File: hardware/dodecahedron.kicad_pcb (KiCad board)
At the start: 2 copper layers, 100 x 86.6 mm, 49 parts, among them J1 Conn_01x04, J2 Conn_01x04, J3 Conn_01x04, J4 Conn_01x04, J5 Conn_01x04, J6 Conn_01x04

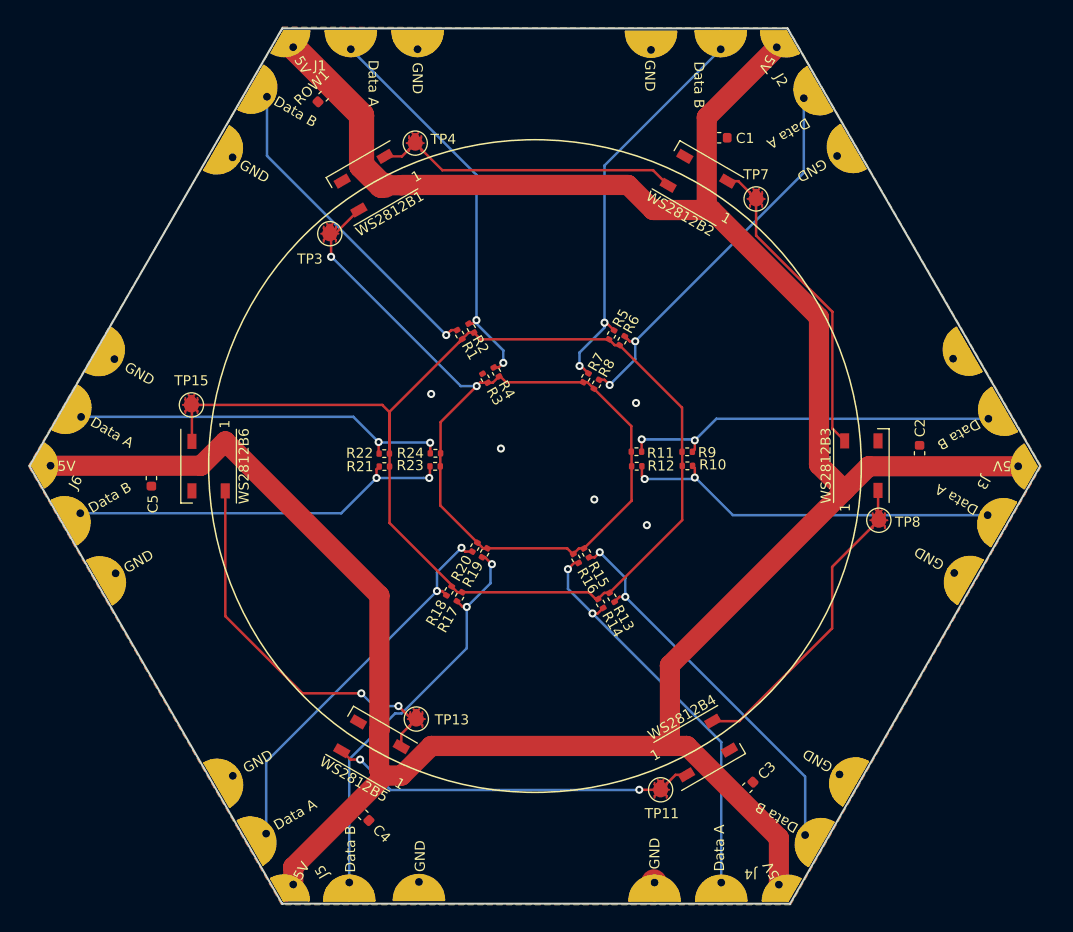
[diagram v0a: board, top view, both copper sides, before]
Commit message: Fixed up a rotated LED
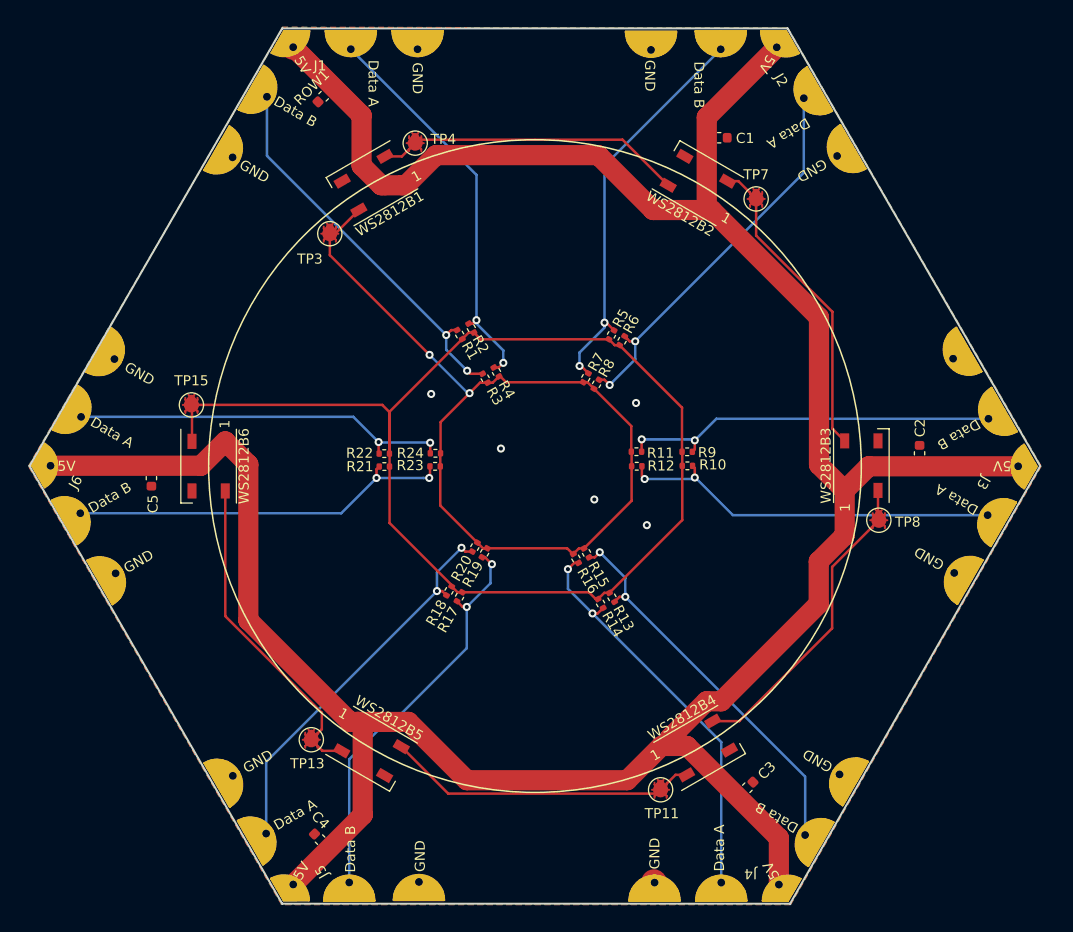
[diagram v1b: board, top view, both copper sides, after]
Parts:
- moved TP13 10.6 mm to (114.1, 162.4)
- moved C4 4.92 mm to (115.0, 172.3), turned to 135 degrees
- turned WS2812B5 to -30 degrees
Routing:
- net +5V: track 275.0 -> 282.1 mm
- net Net-(WS2812B5-DOU): track 38.9 -> 32.5 mm, vias 2 -> 0
- net Net-(J1-Pin_3): track 32.2 -> 38.2 mm, vias 1 -> 2
- net Net-(WS2812B4-DOU): track 36.3 -> 30.9 mm, vias 2 -> 0

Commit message: Added circles to the silk screen
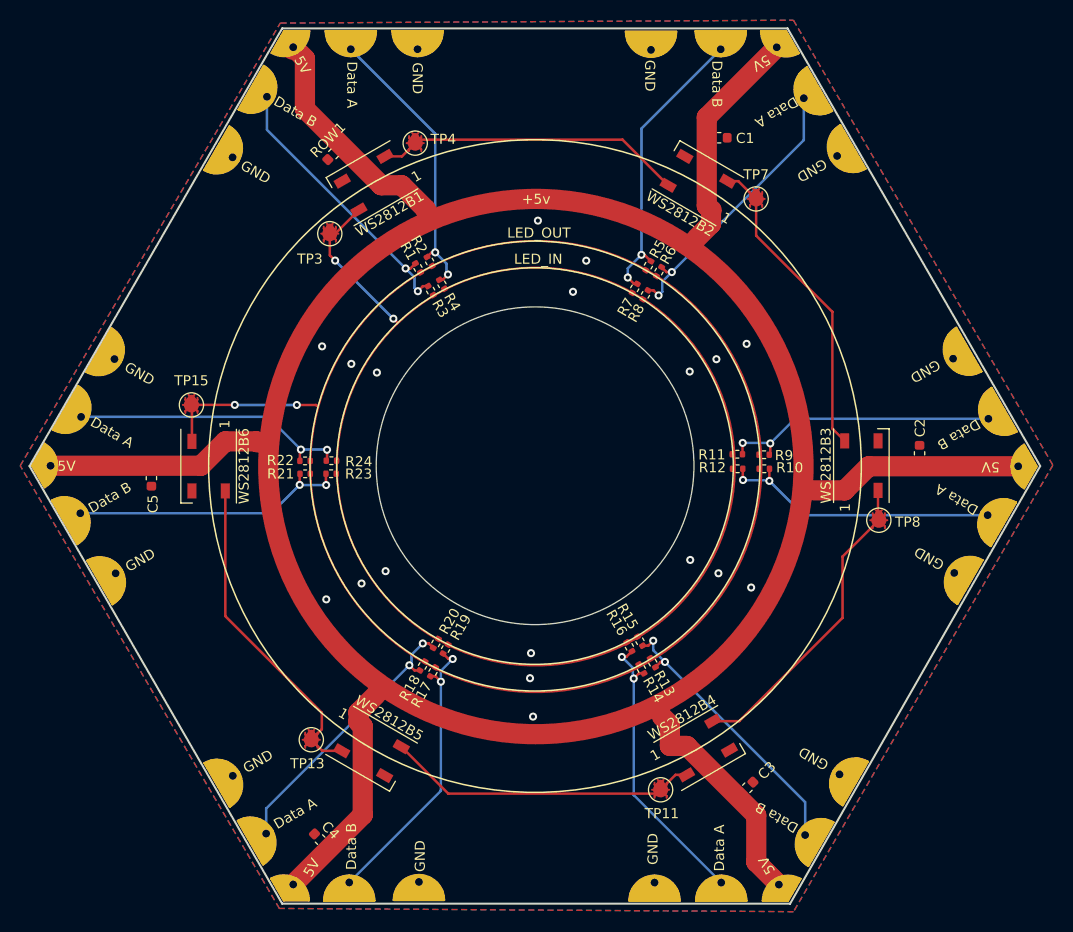
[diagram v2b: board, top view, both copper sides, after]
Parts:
- moved R23 10.3 mm to (116.1, 136.1)
- moved R24 10.3 mm to (116.1, 134.8)
- moved R19 10.3 mm to (127.4, 153.5)
- moved R20 10.3 mm to (126.5, 152.9)
- moved R15 10.2 mm to (146.7, 152.7)
- moved R16 10.2 mm to (145.6, 153.2)
- moved R3 10.2 mm to (125.9, 118.0)
- moved R4 10.2 mm to (127.1, 117.4)
- moved R7 10.1 mm to (146.1, 117.8)
- moved R8 10.1 mm to (147.2, 118.4)
- moved R11 9.98 mm to (156.3, 134.2)
- moved R12 9.98 mm to (156.3, 135.6)
- moved R17 7.88 mm to (126.2, 155.7)
- moved R18 7.88 mm to (125.1, 155.1)
- moved R21 7.87 mm to (113.5, 136.1)
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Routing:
- net +5V: track 282.1 -> 133.1 mm
- net LED_OUT: track 120.3 -> 16.0 mm, vias 0 -> 2
- net LED_IN: track 87.0 -> 15.3 mm
- net Net-(J5-Pin_3): track 40.2 -> 28.8 mm
- net Net-(J2-Pin_2): track 39.2 -> 27.9 mm
- net Net-(J4-Pin_3): track 38.9 -> 27.9 mm
- net Net-(J4-Pin_2): track 39.9 -> 28.8 mm
- net Net-(J1-Pin_2): track 39.3 -> 28.3 mm
- net Net-(J5-Pin_2): track 38.6 -> 27.7 mm
- net Net-(J2-Pin_3): track 39.6 -> 28.8 mm
- net Net-(J6-Pin_3): track 38.4 -> 27.7 mm
- net Net-(J1-Pin_3): track 38.2 -> 27.8 mm
- net Net-(J3-Pin_2): track 38.2 -> 28.0 mm
- net Net-(J3-Pin_3): track 37.7 -> 27.6 mm
- net Net-(J6-Pin_2): track 37.8 -> 28.0 mm
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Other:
- outline, holes or cut-outs redrawn
- board text added: "+5v"
- board text added: "GND"
- board text added: "JLCJLCJLCJLC"
- board text added: "LED_IN"
- board text added: "LED_OUT"
- board text added: "Steven Smethurst (Abluestar.com) Version: 2024-Mar-28 https://github.com/funvill/dodecahedron-pcb"
